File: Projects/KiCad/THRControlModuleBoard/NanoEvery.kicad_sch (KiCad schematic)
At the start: 8 parts, among them IC1 LTC1480CN8#PBF, IC2 LTC1480CN8#PBF, J4 Conn_01x04_Socket, J5 Conn_01x04_Socket, J7 Conn_01x02_Socket, U3 NUCLEO-F303K8

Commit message: KiCADを更新
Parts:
- removed J7: Conn_01x02_Socket, CONNECTOR:CONNECTOR_2-STRAIGHT, symbol Connector:Conn_01x02_Socket
- removed U3: NUCLEO-F303K8, MODULE_NUCLEO-F303K8, symbol NUCLEO-F303K8:NUCLEO-F303K8
- added A1: Arduino_Nano_Every, Module:Arduino_Nano, symbol MCU_Module:Arduino_Nano_Every
- C8, C9: value C -> 0.1; footprint (none) -> Capacitor_SMD:C_0805_2012Metric_Pad1.18x1.45mm_HandSolder
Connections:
- net +12V: now also A1.30 (VIN)
- net GND: now also A1.29 (GND), A1.4 (GND)
- net RS485__DI-TX: now also A1.1 (TX1)
- net RS485__ENABLE: now also A1.5 (D2)
- net RS485__RO-RX: now also A1.2 (RX1)
- net +3.3V renamed NanoEvery_3.3V
- net NanoEvery_3.3V: now also A1.17 (3V3)
- new net MAX31856__DRDY-DRDY: A1.7 (D4)
- new net MAX31856__FAULT-FAULT: A1.8 (D5)
- new net MAX31856__SCK-SCLK: A1.16 (SCK)
- new net MAX31856__SDI-MOSI: A1.14 (MOSI)
- new net MAX31856__SDO-MISO: A1.15 (MISO)
- new net MAX31856__~{CS}-~{CS}: A1.6 (D3)
- no-connect marks 0 -> 3

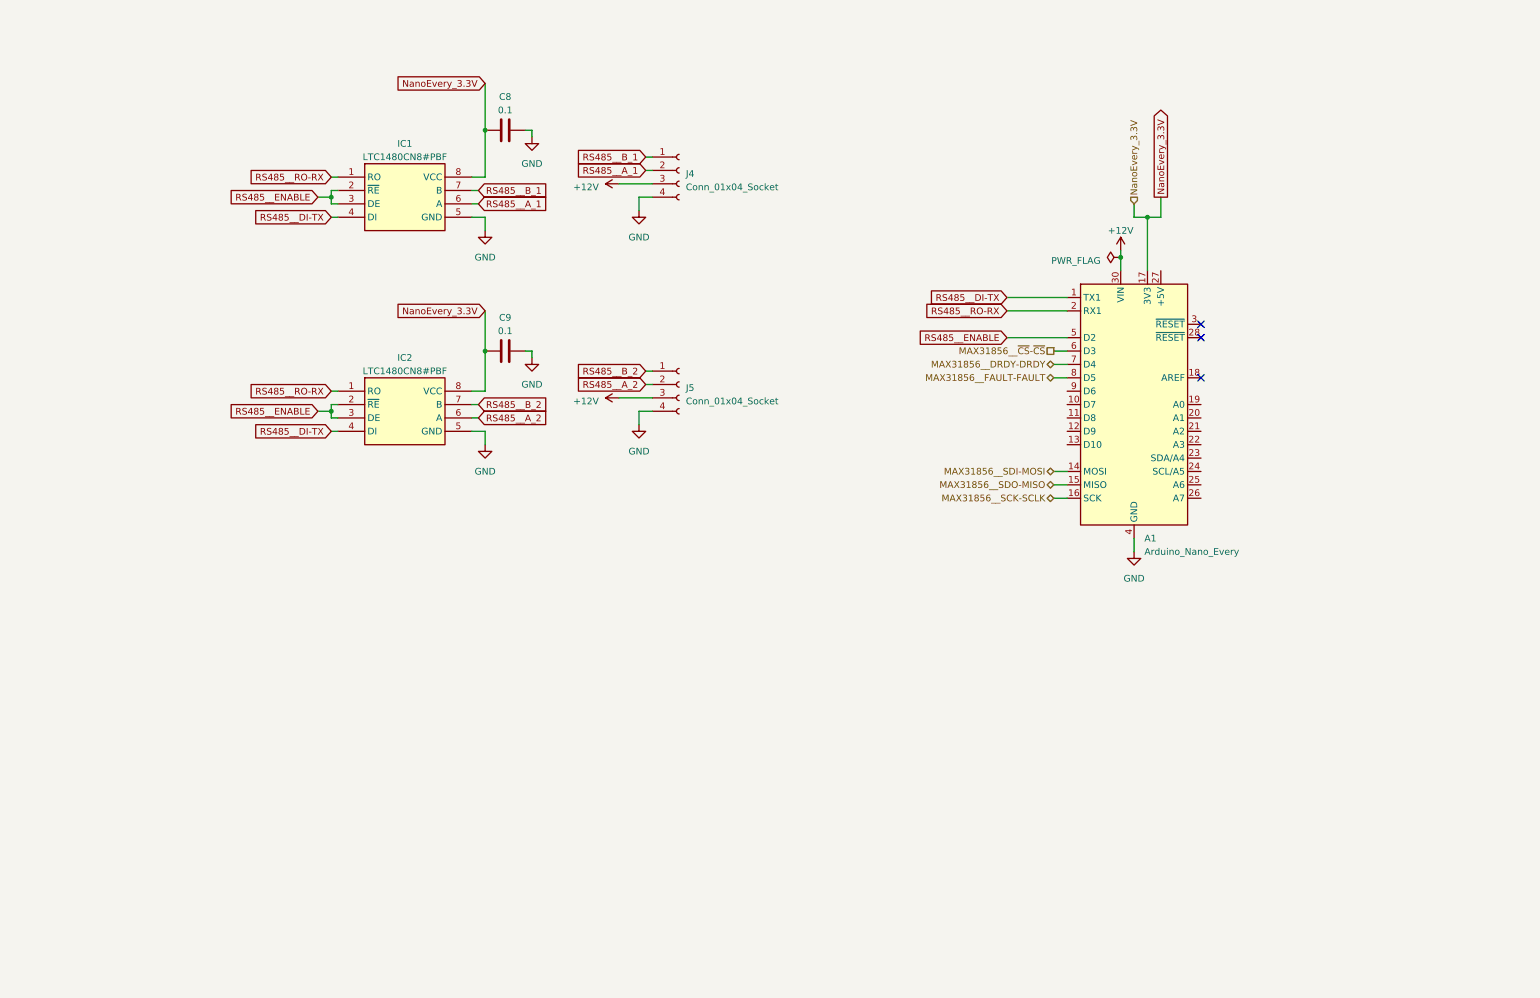
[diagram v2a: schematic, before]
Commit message: MAX31855、CAN、一部コネクタの追加。 基板形状は供給待ち。
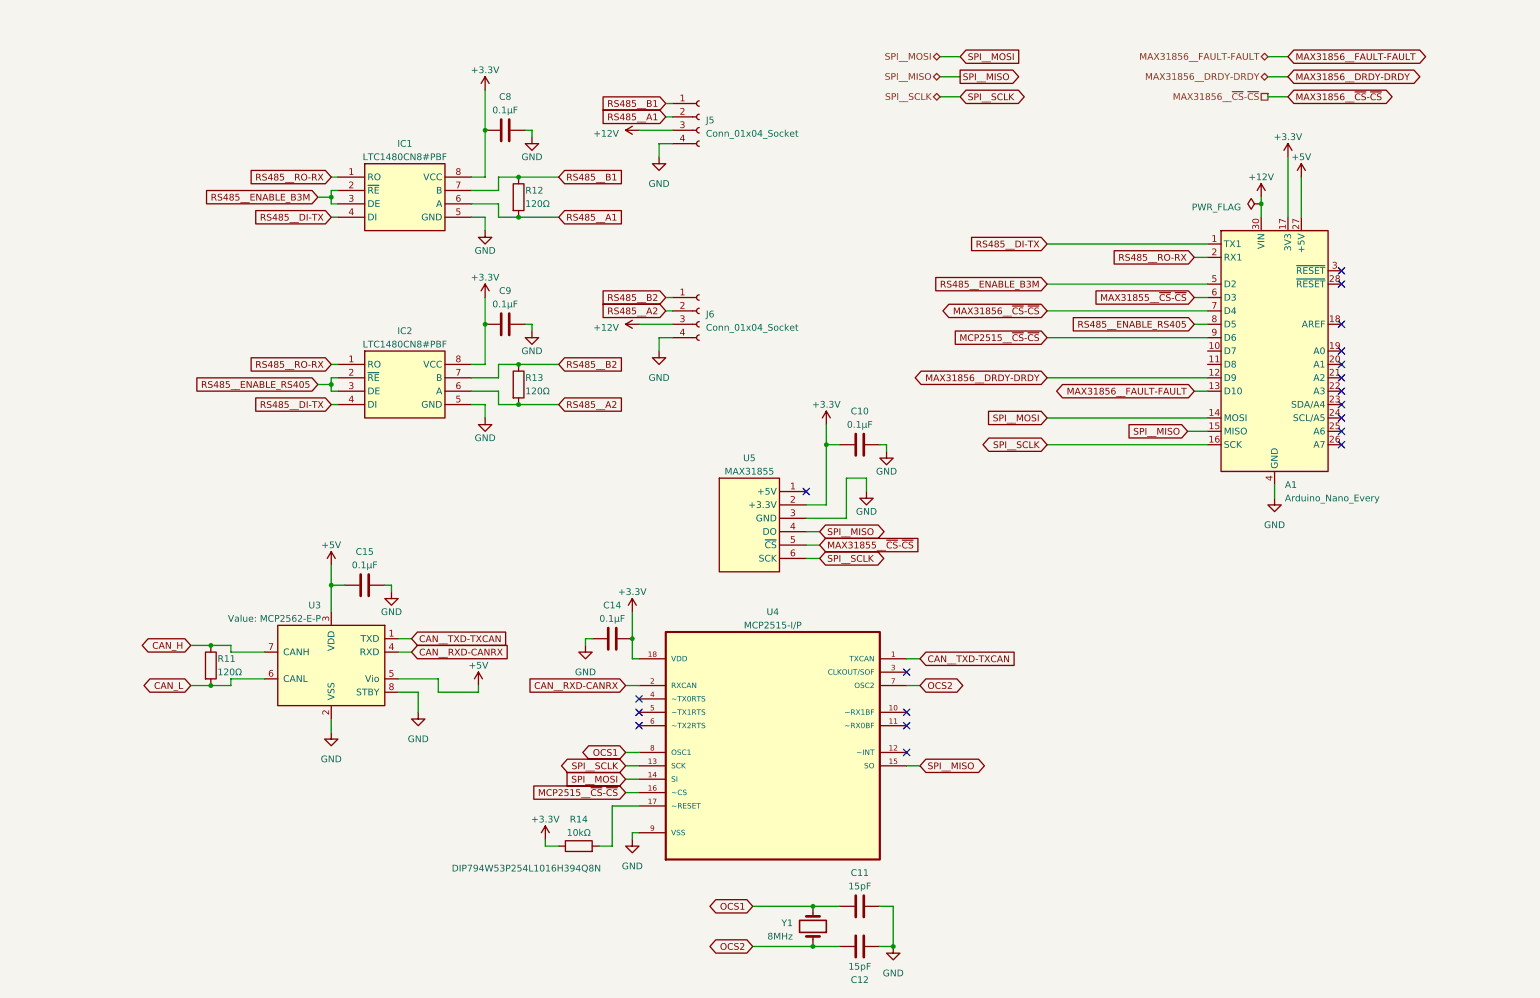
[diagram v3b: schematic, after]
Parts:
- added C10: 0.1μF, Capacitor_SMD:C_0603_1608Metric_Pad1.08x0.95mm_HandSolder, symbol Device:C
- added C11, C12: 15pF, Capacitor_SMD:C_0603_1608Metric_Pad1.08x0.95mm_HandSolder, symbol Device:C
- added C14, C15: 0.1μF, Capacitor_SMD:C_0805_2012Metric_Pad1.18x1.45mm_HandSolder, symbol Device:C
- added R11, R12, R13: 120Ω, Resistor_SMD:R_0603_1608Metric_Pad0.98x0.95mm_HandSolder, symbol Device:R
- added R14: 10kΩ, Resistor_SMD:R_0603_1608Metric_Pad0.98x0.95mm_HandSolder, symbol Device:R
- added U3: MCP2562-E-P, Package_DIP:DIP-8_W7.62mm, symbol Interface_CAN_LIN:MCP2562-E-P
- added U4: MCP2515-I/P, DIP254P762X432-18, symbol MCP2515-I_P:MCP2515-I/P
- added U5: MAX31855, MAX31855:MAX31855, symbol MAX31855:MAX31855
- added Y1: 8MHz, Crystal:Crystal_HC49-U_Vertical, symbol Device:Crystal
- C8, C9: value 0.1 -> 0.1μF
- renumbered J4 to J5, J5 to J6
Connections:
- net GND: now also C10.2, C11.2, C12.2, C14.2, C15.1, U3.2 (VSS), U3.8 (STBY), U4.9 (VSS), U5.3 (GND)
- net MAX31856__DRDY-DRDY: now also A1.12 (D9); no longer A1.7 (D4)
- net MAX31856__FAULT-FAULT: now also A1.13 (D10); no longer A1.8 (D5)
- net MAX31856__~{CS}-~{CS}: now also A1.7 (D4); no longer A1.6 (D3)
- net +5V: now reaches A1.27 (+5V)
- net +5V: now also C15.2, U3.3 (VDD), U3.5 (Vio)
- net MCP2515__~{CS}-~{CS}: now reaches A1.9 (D6)
- net MCP2515__~{CS}-~{CS}: now also U4.16 (~CS)
- net MAX31856__SCK-SCLK renamed SPI__SCLK
- net SPI__SCLK: now also U4.13 (SCK), U5.6 (SCK)
- net MAX31856__SDI-MOSI renamed SPI__MOSI
- net SPI__MOSI: now also U4.14 (SI)
- net MAX31856__SDO-MISO renamed SPI__MISO
- net SPI__MISO: now also U4.15 (SO), U5.4 (DO)
- net NanoEvery_3.3V renamed +3.3V
- net +3.3V: now also C10.1, C14.1, R14.1, U4.18 (VDD), U5.2 (+3.3V)
- net RS485__A_1 renamed RS485__A1
- net RS485__A1: now also R12.2
- net RS485__A_2 renamed RS485__A2
- net RS485__A2: now also R13.2
- net RS485__B_1 renamed RS485__B1
- net RS485__B1: now also R12.1
- net RS485__B_2 renamed RS485__B2
- net RS485__B2: now also R13.1
- net RS485__ENABLE renamed RS485__ENABLE_B3M
- net RS485__ENABLE_B3M: no longer IC2.2 (~{RE}), IC2.3 (DE)
- new net: R14.2, U4.17 (~RESET)
- new net CAN_H: R11.1, U3.7 (CANH)
- new net CAN_L: R11.2, U3.6 (CANL)
- new net CAN__RXD-CANRX: U3.4 (RXD), U4.2 (RXCAN)
- new net CAN__TXD-TXCAN: U3.1 (TXD), U4.1 (TXCAN)
- new net MAX31855__~{CS}-~{CS}: A1.6 (D3), U5.5 (~{CS})
- new net OCS1: C11.1, U4.8 (OSC1), Y1.2
- new net OCS2: C12.1, U4.7 (OSC2), Y1.1
- new net RS485__ENABLE_RS405: A1.8 (D5), IC2.2 (~{RE}), IC2.3 (DE)
- no-connect marks 3 -> 19
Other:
- moved on the sheet: A1, C9, IC2, J5, J6

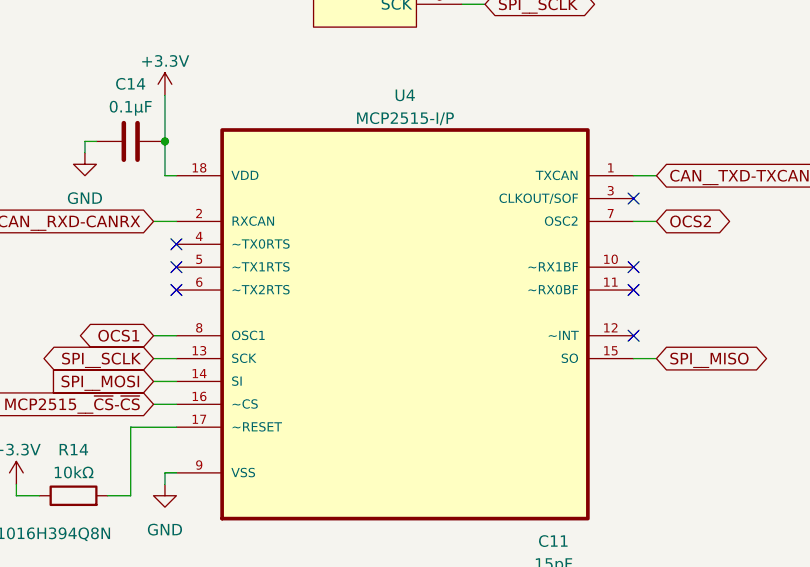
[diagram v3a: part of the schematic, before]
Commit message: PCBにQRコードを追加
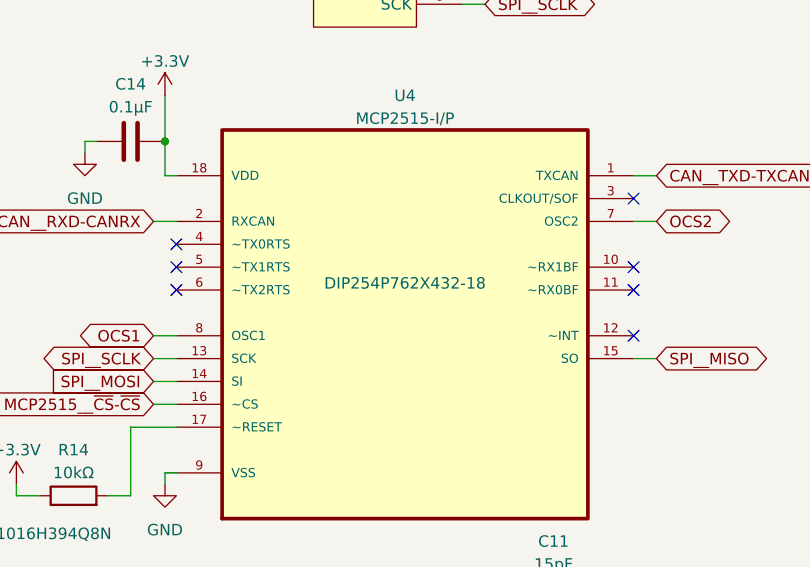
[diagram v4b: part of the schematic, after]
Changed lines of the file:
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@@
     )
     (property "Footprint" "DIP254P762X432-18" (at 135.89 144.78 0)
-      (effects (font (size 1.27 1.27)) (justify bottom) hide)
+      (effects (font (size 1.27 1.27)) (justify bottom))
     )
     (property "Datasheet" "" (at 135.89 144.78 0)

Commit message: 外形を大方決めた
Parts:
- added C13, C14, C15, C16, C17, C18: 0.1u, Capacitor_SMD:C_0805_2012Metric_Pad1.18x1.45mm_HandSolder, symbol Device:C
- added D4: D, Diode_SMD:D_SOD-123, symbol Device:D
- added LS1: PKB24SPCH3601-B0, PKB24SPCH3601-B0:SPKR_PKB24SPCH3601-B0, symbol PKB24SPCH3601-B0:PKB24SPCH3601-B0
- added R10: 300, Resistor_SMD:R_0603_1608Metric_Pad0.98x0.95mm_HandSolder, symbol Device:R
- added R11, R13, R14, R15, R16, R17, R18, R19, R20, R21: 10k, Resistor_SMD:R_0603_1608Metric_Pad0.98x0.95mm_HandSolder, symbol Device:R
- added R12, R22, R23, R24, R25, R26: 1k, Resistor_SMD:R_0603_1608Metric_Pad0.98x0.95mm_HandSolder, symbol Device:R
- added U4: TLP222A, Package_DIP:DIP-4_W7.62mm, symbol Relay_SolidState:TLP222A
- C12: renamed from C10; value 0.1μF -> 0.1μ
- C6: renamed from C15; value 0.1μF -> 0.1u; footprint Capacitor_SMD:C_0805_2012Metric_Pad1.18x1.45mm_HandSolder -> Capacitor_SMD:C_0603_1608Metric_Pad1.08x0.95mm_HandSolder
- C7: renamed from C8; value 0.1μF -> 0.1u; footprint Capacitor_SMD:C_0805_2012Metric_Pad1.18x1.45mm_HandSolder -> Capacitor_SMD:C_0603_1608Metric_Pad1.08x0.95mm_HandSolder
- C8: renamed from C9; value 0.1μF -> 0.1u; footprint Capacitor_SMD:C_0805_2012Metric_Pad1.18x1.45mm_HandSolder -> Capacitor_SMD:C_0603_1608Metric_Pad1.08x0.95mm_HandSolder
- C9: renamed from C14; value 0.1μF -> 0.1u; footprint Capacitor_SMD:C_0805_2012Metric_Pad1.18x1.45mm_HandSolder -> Capacitor_SMD:C_0603_1608Metric_Pad1.08x0.95mm_HandSolder
- IC1, IC2: footprint DIP794W53P254L1016H394Q8N -> LTC1480CN8#PBF:DIP794W53P254L1016H394Q8N
- R6: renamed from R11; value 120Ω -> 120
- R7: renamed from R12; value 120Ω -> 120
- R8: renamed from R13; value 120Ω -> 120
- R9: renamed from R14; value 10kΩ -> 10k
- U3: renamed from U4; footprint DIP254P762X432-18 -> MCP2515-I_P:DIP254P762X432-18
- renumbered C11 to C10, C12 to C11, U3 to U2
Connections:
- net +12V: now also D4.2 (A), LS1.P, U4.4; no longer A1.30 (VIN)
- net +5V: now also R13.2, R14.2, R15.2, R16.2
- net GND: now also C13.2, C14.2, C15.2, C16.2, C17.2, C18.2, LS1.N, U4.2, U4.3
- net MAX31855__~{CS}-~{CS}: now also A1.8 (D5); no longer A1.6 (D3)
- net RS485__ENABLE_RS405: now also A1.6 (D3); no longer A1.8 (D5)
- net Umbilical__launchPin: now reaches A1.10 (D7)
- net Umbilical__launchPin: now also R22.2
- net Umbilical__waitingPin: now reaches A1.11 (D8)
- net Umbilical__waitingPin: now also R23.2
- net B3M_Servo__Open: now reaches A1.19 (A0)
- net B3M_Servo__Open: now also R24.2
- net B3M_Servo__Close: now reaches A1.20 (A1)
- net B3M_Servo__Close: now also R25.2
- net RS405_Servo__Open: now reaches A1.21 (A2)
- net RS405_Servo__Open: now also R12.2
- net RS405_Servo__Close: now reaches A1.22 (A3)
- net RS405_Servo__Close: now also R26.2
- net IO__Busser: now reaches A1.25 (A6)
- net IO__Busser: now also R10.1
- net CAN_H renamed CAN__H
- net CAN_L renamed CAN__L
- new net: C17.1, R20.2, R25.1
- new net: R10.2, U4.1
- new net: C16.1, R19.2, R24.1
- new net: C15.1, R18.2, R23.1
- new net: C18.1, R21.2, R26.1
- new net: C14.1, R17.2, R22.1
- new net: A1.30 (VIN), D4.1 (K)
- new net: C13.1, R11.2, R12.1
- new net B3M_Servo__Closeinput: R16.1, R20.1
- new net B3M_Servo__Openinput: R15.1, R19.1
- new net RS405_Servo__Closeinput: R21.1
- new net RS405_Servo__Openinput: R11.1
- new net Umbilical__launchInput: R13.1, R17.1
- new net Umbilical__waitingInput: R14.1, R18.1
- no-connect marks 19 -> 14
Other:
- note added: "MAX31855 熱電対-デジタルコンバーター"
- moved on the sheet: A1, C12, C6, C7, C8, IC1, IC2, J5, J6, R6, R7, R8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
